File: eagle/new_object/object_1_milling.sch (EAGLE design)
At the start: 13 parts, among them U1 GY-521MPU6050

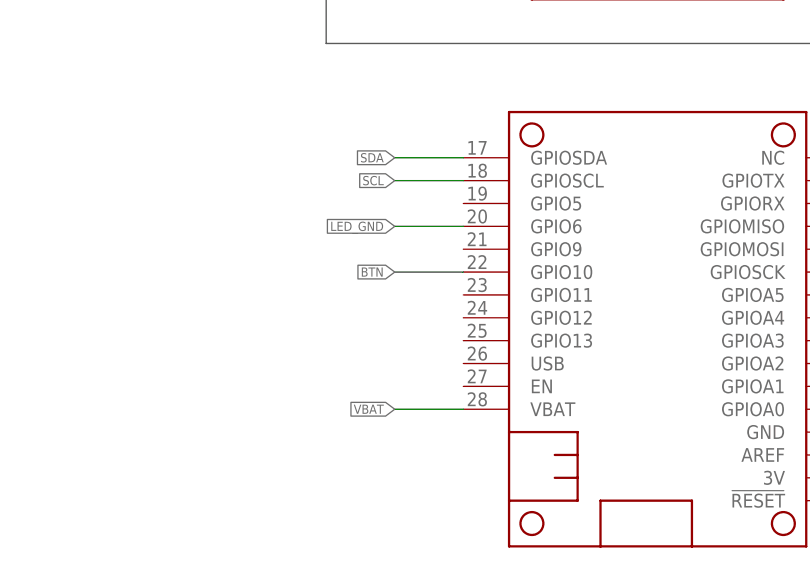
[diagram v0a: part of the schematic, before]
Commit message: Change switch to pin 23, clean the mess git did with the files
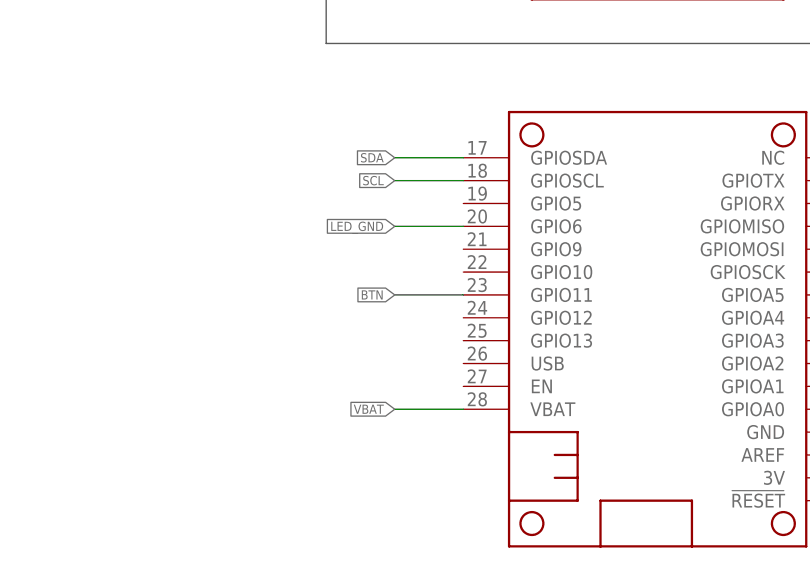
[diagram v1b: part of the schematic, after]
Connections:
- net BTN: now also MS1.GPIO11; no longer MS1.GPIO10
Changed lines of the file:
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@@
 <net name="BTN" class="0">
-<segment>
-<pinref part="MS1" gate="G$1" pin="GPIO10"/>
-<wire x1="88.9" y1="93.98" x2="81.28" y2="93.98" width="0.1524" layer="91"/>
-<label x="81.28" y="93.98" size="1.016" layer="95" rot="R180" xref="yes"/>
-</segment>
 <segment>
 <pinref part="JP1" gate="A" pin="3"/>
@@
 <label x="27.94" y="114.3" size="1.016" layer="95" xref="yes"/>
 </segment>
+<segment>
+<pinref part="MS1" gate="G$1" pin="GPIO11"/>
+<wire x1="88.9" y1="91.44" x2="81.28" y2="91.44" width="0.1524" layer="91"/>
+<label x="81.28" y="91.44" size="1.016" layer="95" rot="R180" xref="yes"/>
+</segment>
 </net>
